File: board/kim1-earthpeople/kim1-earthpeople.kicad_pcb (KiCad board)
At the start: 2 copper layers, 111 x 53.3 mm, 10 parts, among them J101 Conn_02x18_Odd_Even, J102 Conn_02x20_Odd_Even, P2 Power, P3 XIO_4, P4 XIO_2, P5 XIO_1, P6 XIO_3, P7 XIO_5

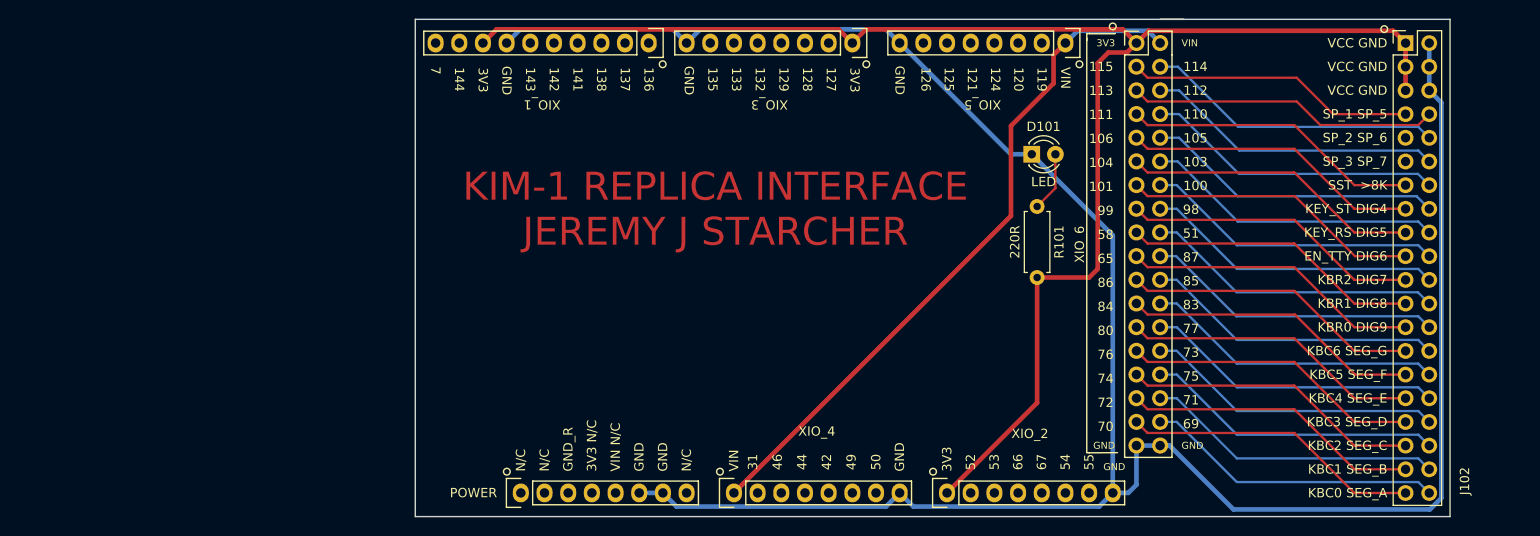
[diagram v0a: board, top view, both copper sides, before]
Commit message: Added the serial connection -- oops.
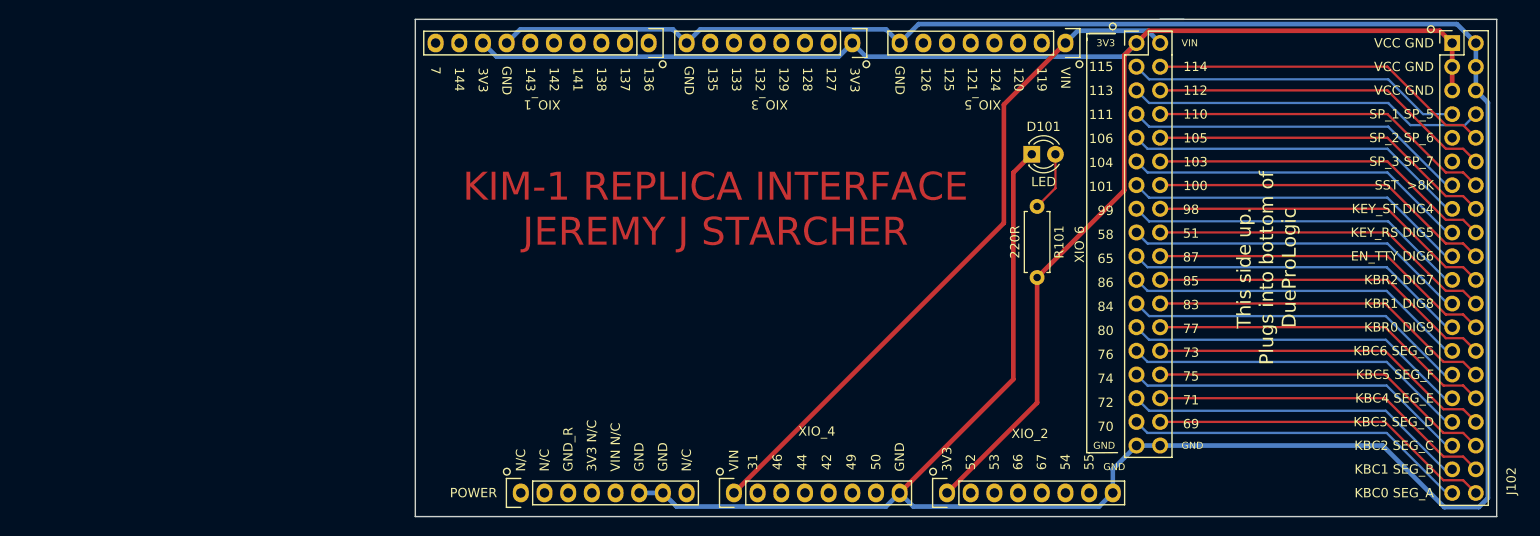
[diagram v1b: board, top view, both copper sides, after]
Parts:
- moved J102 5.00 mm to (231.2, 70.9)
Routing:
- net GND: track 249.3 -> 299.8 mm
- net SST_KEY: track 32.0 -> 37.0 mm
- net RS_KEY: track 32.0 -> 37.0 mm
- net LED_SEG_6: track 32.0 -> 37.0 mm
- net KB_ROW_1: track 32.0 -> 37.0 mm
- net KB_COL_6: track 32.0 -> 37.0 mm
- net KB_COL_4: track 32.0 -> 37.0 mm
- net LED_DIG_7: track 32.0 -> 37.0 mm
- net LED_DIG_6: track 32.0 -> 37.0 mm
- net KB_ROW_2: track 32.0 -> 37.0 mm
- net KB_ROW_0: track 32.0 -> 37.0 mm
- net KB_COL_3: track 32.0 -> 37.0 mm
- net KB_COL_2: track 32.0 -> 37.0 mm
- net KB_COL_1: track 32.0 -> 37.0 mm
- net KB_COL_0: track 32.0 -> 37.0 mm
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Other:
- board size 111 x 53.3 mm -> 116 x 53.3 mm
- board text added: "This side up. Plugs into bottom of DueProLogic"

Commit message: Updated the PCB with more labels and to be cleaner.
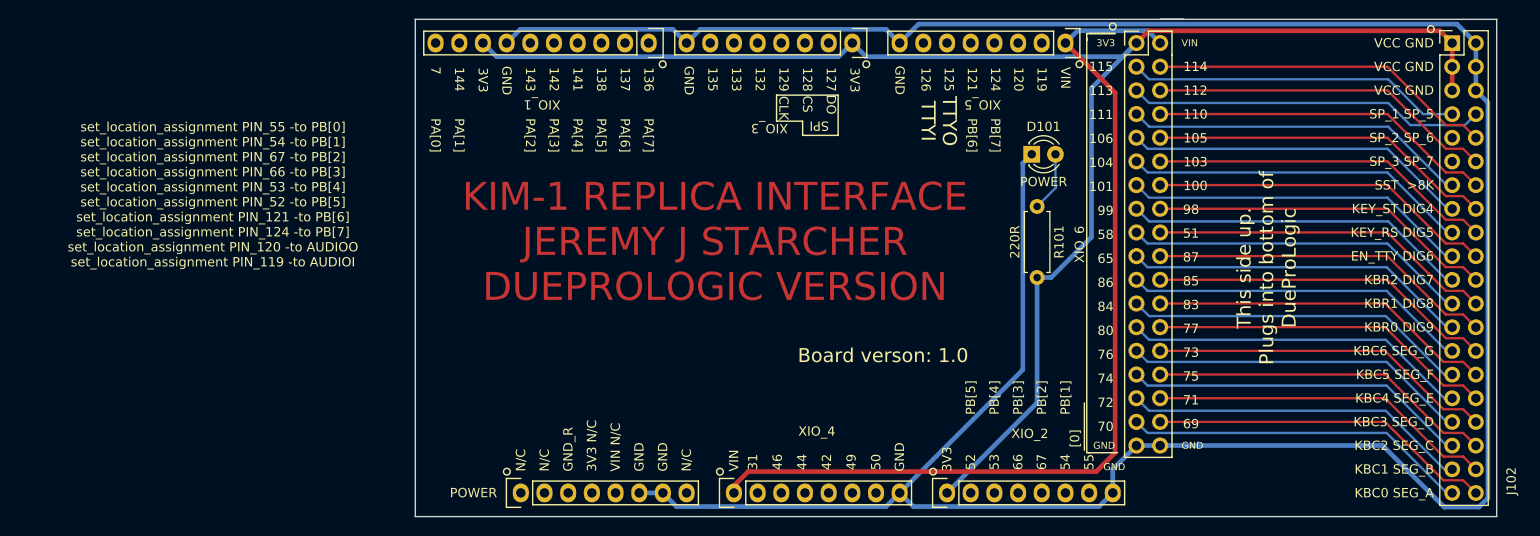
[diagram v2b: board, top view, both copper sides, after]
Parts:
- D101: value LED -> POWER
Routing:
- net 5V: track 74.2 -> 100.5 mm
- net 3V3: track 169.2 -> 170.1 mm
- net ENABLE_TTY: track 37.0 -> 36.4 mm
- net SST_KEY: track 37.0 -> 36.4 mm
- net KB_ROW_2: track 37.0 -> 36.4 mm
- net KB_ROW_0: track 37.0 -> 36.4 mm
- net KB_COL_6: track 37.0 -> 36.4 mm
- net KB_COL_3: track 37.0 -> 36.4 mm
- net KB_COL_2: track 37.0 -> 36.4 mm
- net KB_COL_0: track 37.0 -> 36.4 mm
- net ST_KEY: track 37.0 -> 36.5 mm
- net RS_KEY: track 37.0 -> 36.5 mm
- net KB_ROW_1: track 37.0 -> 36.5 mm
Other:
- board text added: "Board verson: 1.0"
- board text added: "CLK"
- board text added: "CS"
- board text added: "DO"
- board text added: "KIM-1 REPLICA INTERFACE JEREMY J STARCHER DUEPROLOGIC VERSION"
- board text added: "PA[0]"
- board text added: "PA[1]"
- board text added: "PA[2]"
- board text added: "PA[3]"
- board text added: "PA[4]"
- board text added: "PA[5]"
- board text added: "PA[6]"
- board text added: "PA[7]"
- board text added: "PB[1]"
- board text added: "PB[2]"
- board text added: "PB[3]"
- board text added: "PB[4]"
- board text added: "PB[5]"
- board text added: "PB[6]"
- board text added: "PB[7]"
- board text added: "SPI"
- board text added: "TTYI"
- board text added: "TTYO"
- board text added: "[0]"
- board text added: "set_location_assignment PIN_55 -to PB[0]r set_location_assignment PIN_54 -to PB[1]r set_location_assignment PIN_67 -to PB[2]r set_location_assignment PIN_66 -to PB[3]r set_location_assignment PIN_53 -to PB[4]r set_location_assignment PIN_52 -to PB[5]r set_location_assignment PIN_121 -to PB[6]r set_location_assignment PIN_124 -to PB[7]r set_location_assignment PIN_120 -to AUDIOOr set_location_assi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"
- board text removed: "KIM-1 REPLICA INTERFACE JEREMY J STARCHER"
